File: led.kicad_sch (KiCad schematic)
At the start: 5 parts, among them J4 Conn_01x02_Pin, Q2 IRLML6402, U7 TC4428xOA

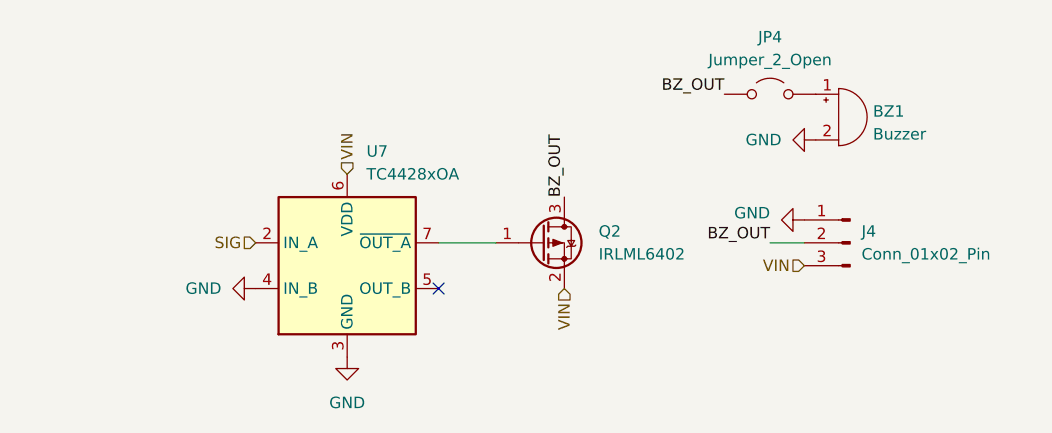
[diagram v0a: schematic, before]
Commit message: Add leds, docs cleanup
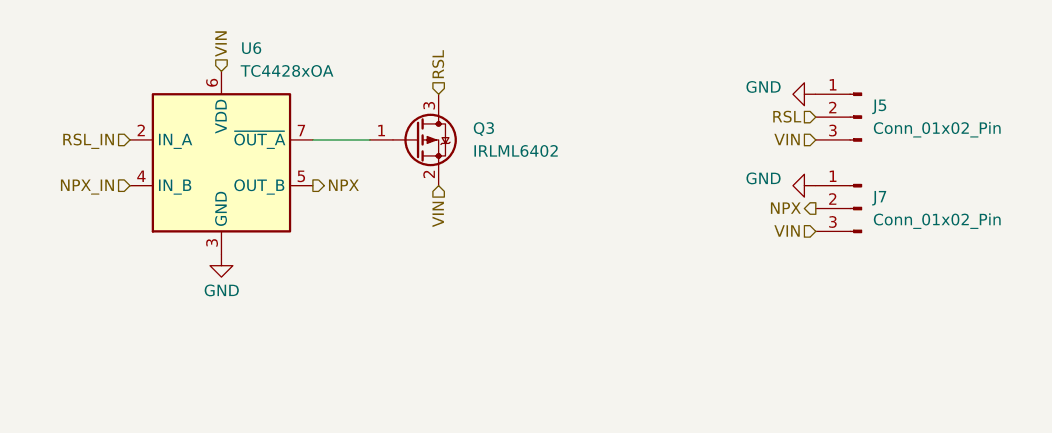
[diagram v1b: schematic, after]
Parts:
- removed BZ1: Buzzer, Buzzer_Beeper:Buzzer_TDK_PS1240P02BT_D12.2mm_H6.5mm, symbol Device:Buzzer
- removed J4: Conn_01x02_Pin, Connector_Molex:Molex_Nano-Fit_105309-xx03_1x03_P2.50mm_Vertical, symbol Connector:Conn_01x03_Pin
- removed JP4: Jumper_2_Open, Connector_PinHeader_2.00mm:PinHeader_1x02_P2.00mm_Vertical, symbol Jumper:Jumper_2_Open
- removed Q2: IRLML6402, Package_TO_SOT_SMD:SOT-23, symbol Transistor_FET:IRLML6402
- removed U7: TC4428xOA, Package_SO:SOIC-8_3.9x4.9mm_P1.27mm, symbol Driver_FET:TC4428xOA
- added J5, J7: Conn_01x02_Pin, Connector_Molex:Molex_Nano-Fit_105309-xx03_1x03_P2.50mm_Vertical, symbol Connector:Conn_01x03_Pin
- added Q3: IRLML6402, Package_TO_SOT_SMD:SOT-23, symbol Transistor_FET:IRLML6402
- added U6: TC4428xOA, Package_SO:SOIC-8_3.9x4.9mm_P1.27mm, symbol Driver_FET:TC4428xOA
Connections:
- net GND: now also J5.1 (Pin_1), J7.1 (Pin_1), U6.3 (GND)
- net VIN: now also J5.3 (Pin_3), J7.3 (Pin_3), Q3.2 (S), U6.6 (VDD)
- new net: Q3.1 (G), U6.7 (~{OUT_A})
- new net NPX: J7.2 (Pin_2), U6.5 (OUT_B)
- new net NPX_IN: U6.4 (IN_B)
- new net RSL: J5.2 (Pin_2), Q3.3 (D)
- new net RSL_IN: U6.2 (IN_A)
- no-connect marks 1 -> 0

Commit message: sch, pcb: update pn fields
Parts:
- J5, J7: Part Number (none) -> 1053091103
- Q3: Part Number (none) -> IRLML6402TRPBF
- U6: Part Number (none) -> TC4428EOA713
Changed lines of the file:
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@@
+			)
+		)
+		(property "Part Number" "IRLML6402TRPBF"
+			(at 105.41 97.79 0)
+			(effects
+				(font
+					(size 1.27 1.27)
+				)
+				(hide yes)
 			)
 		)
@@
 			)
 		)
+		(property "Part Number" "1053091103"
+			(at 154.94 105.41 0)
+			(effects
+				(font
+					(size 1.27 1.27)
+				)
+				(hide yes)
+			)
+		)
 		(pin "2"
 		)
@@
 			)
 		)
+		(property "Part Number" "1053091103"
+			(at 154.94 95.25 0)
+			(effects
+				(font
+					(size 1.27 1.27)
+				)
+				(hide yes)
+			)
+		)
 		(pin "2"
 		)
@@
 			(effects
 				(font
+					(size 1.27 1.27)
+				)
+				(hide yes)
+			)
+		)
+		(property "Part Number" "TC4428EOA713"
+			(at 83.82 100.33 0)
+			(effects
+				(font

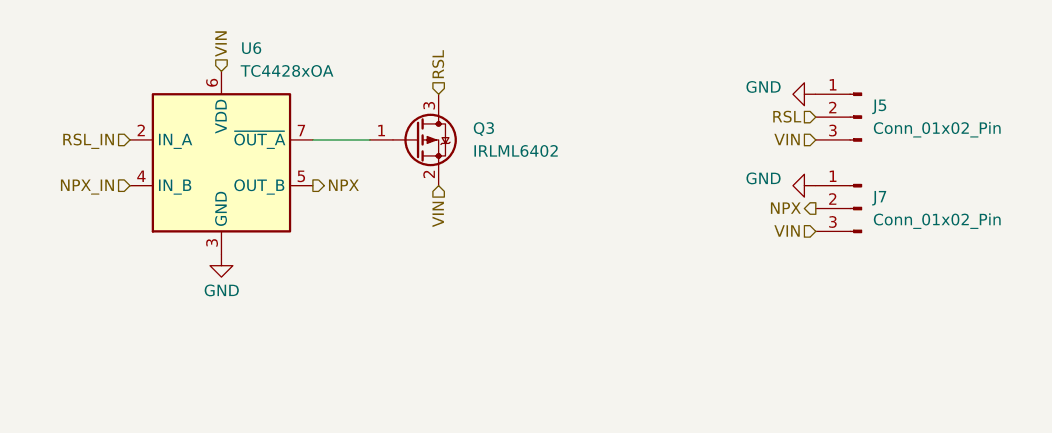
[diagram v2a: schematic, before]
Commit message: rs422, led, pcbs: status leds, readme: add image
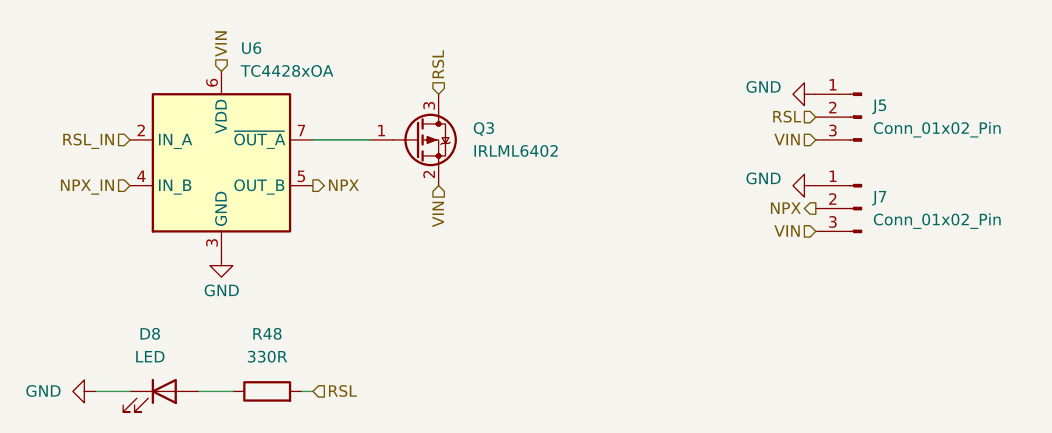
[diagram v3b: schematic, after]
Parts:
- added D8: LED, LED_SMD:LED_0603_1608Metric, symbol Device:LED
- added R48: 330R, Resistor_SMD:R_0603_1608Metric, symbol Device:R
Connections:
- net GND: now also D8.1 (K)
- net RSL: now also R48.2
- new net: D8.2 (A), R48.1
